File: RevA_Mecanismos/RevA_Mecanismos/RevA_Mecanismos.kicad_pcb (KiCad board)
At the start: 4 copper layers, 80 x 80 mm, 84 parts, among them IC1 MAX33040EAKA+T, J1 PROG, J10 Conn_01x02_Pin, J2 Conn_01x03_Pin, J3 430450224, J4 430450224, J5 DEBUG_CONN, J6 430450224, J7 430450224, J8 Conn_01x08_Pin, J9 Conn_01x02_Pin, Q1 NDS352AP, SW1 SW_Push, U1 STM32L431RCTx, U2 R-78E3.3-1.0, U3 R-78E5.0-1.0, Y1 16MHz

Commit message: Adiciones a secciones de motores y power supply para placa de mecanismos
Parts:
- moved G*** 7.66 mm to (203.2, 129.5)
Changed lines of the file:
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@@
   )
   (footprint "footprints:sticker" (layer "B.Cu")
-    (at 203.7 121.9 180)
+    (at 203.2 129.54 180)
     (attr board_only exclude_from_pos_files exclude_from_bom)
     (fp_text reference "G***" (at 0 0) (layer "B.SilkS") hide

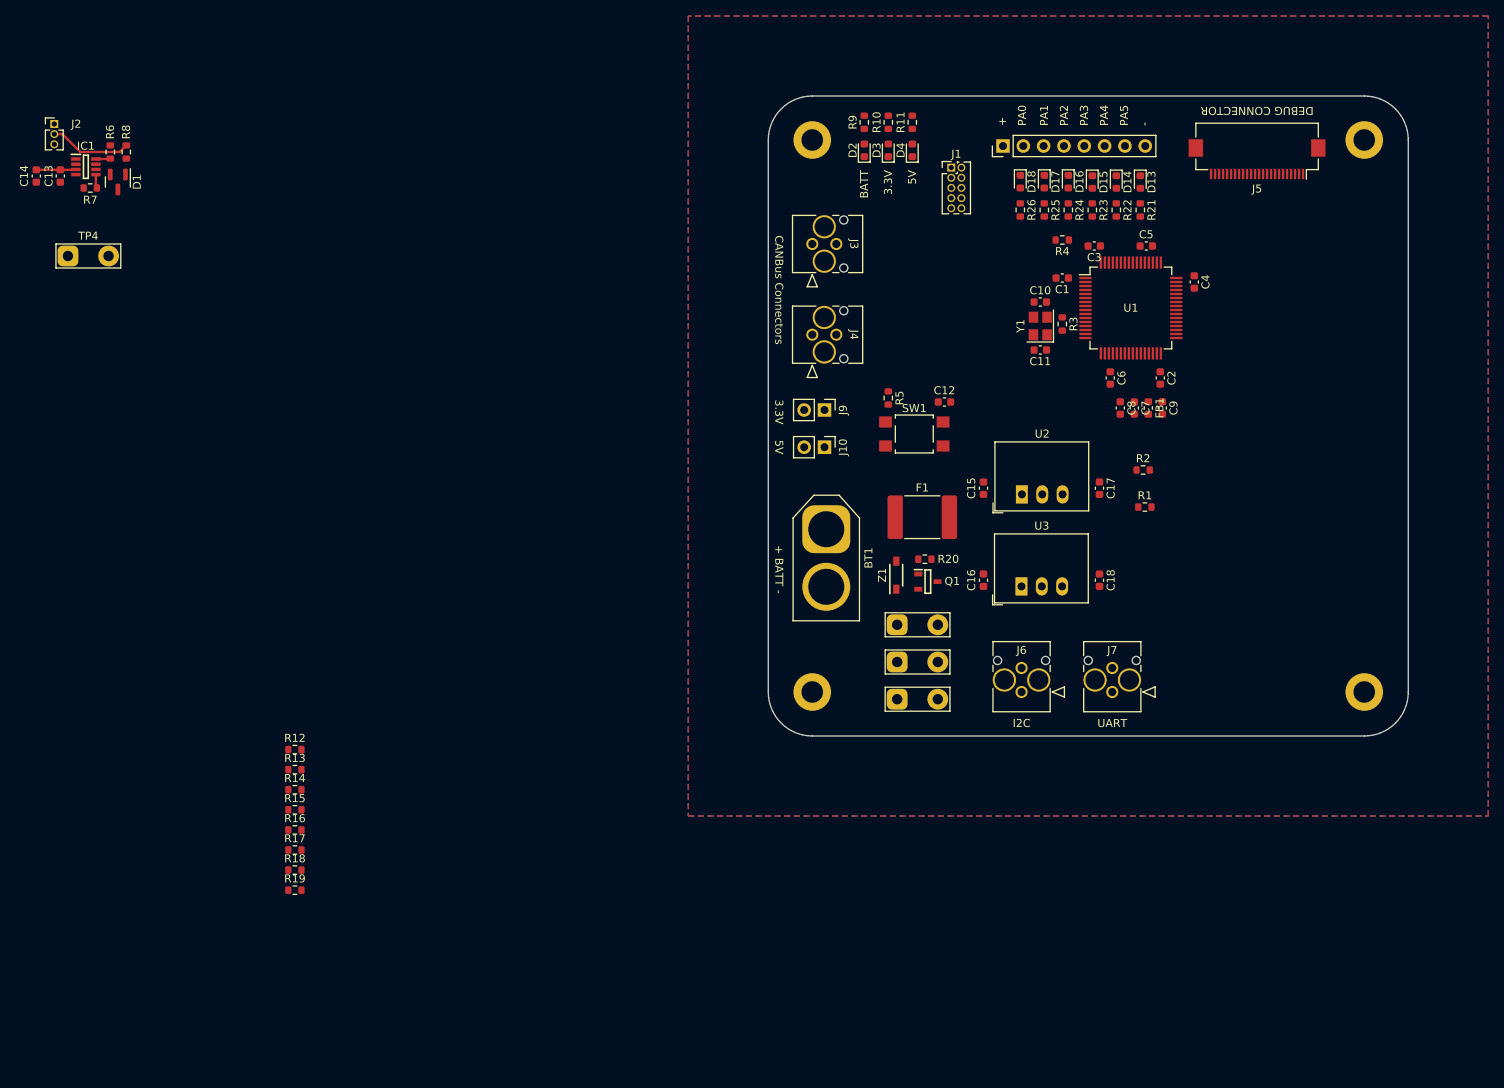
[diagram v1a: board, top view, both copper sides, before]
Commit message: Updated STM32 USV Mechanism PCB
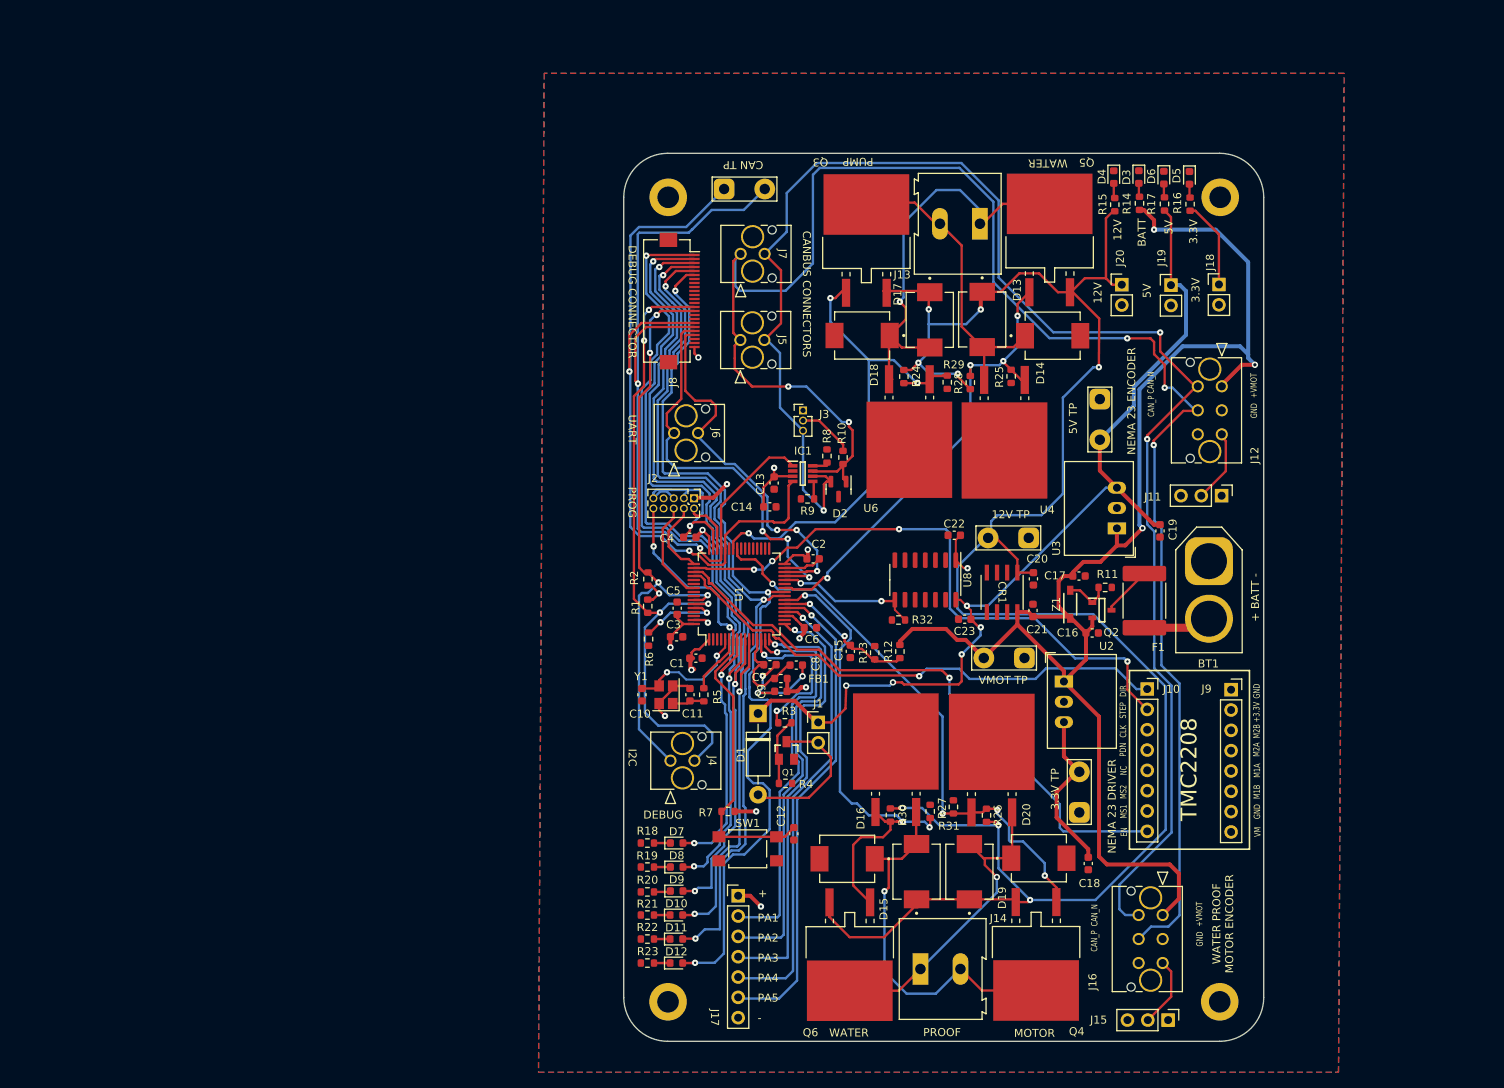
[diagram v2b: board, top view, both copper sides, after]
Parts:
- removed the J8 at (154.3, 31.2)
- removed the R14 at (65.8, 111.7)
- removed the R16 at (65.8, 116.7)
- removed the R17 at (65.8, 119.2)
- removed the R18 at (65.8, 121.8)
- removed the R19 at (65.8, 124.3)
- added C15: 3.3u, Capacitor_SMD:C_0603_1608Metric, F.Cu at (135.3, 94.4)
- added C20: 0.1u, Capacitor_SMD:C_0603_1608Metric, F.Cu at (158.1, 85.4)
- added C21: 0.33u, Capacitor_SMD:C_0603_1608Metric, F.Cu at (158.1, 89.3)
- added C22: 0.1u, Capacitor_SMD:C_0603_1608Metric, F.Cu at (148.2, 79.9)
- added C23: 0.1u, Capacitor_SMD:C_0603_1608Metric, F.Cu at (149.6, 90.4)
- added CR1: L78L12ABD-TR, L78L12ABD-TR:SO-8_STM, F.Cu at (154.2, 87.0)
- added D1: 1N4001, Diode_THT:D_DO-41_SOD81_P10.16mm_Horizontal, F.Cu at (123.7, 102.2)
- added D13: SS34, SS34:DIOM7959X265N, F.Cu at (151.7, 52.9)
- added D14: SS34, SS34:DIOM7959X265N, F.Cu at (160.5, 55.0)
- added D15: SS34, SS34:DIOM7959X265N, F.Cu at (143.5, 122.0)
- added D16: SS34, SS34:DIOM7959X265N, F.Cu at (134.9, 120.4)
- added D17: SS34, SS34:DIOM7959X265N, F.Cu at (145.2, 53.0)
- added D18: SS34, SS34:DIOM7959X265N, F.Cu at (136.7, 54.9)
- added D19: SS34, SS34:DIOM7959X265N, F.Cu at (150.1, 122.0)
- added D20: SS34, SS34:DIOM7959X265N, F.Cu at (158.8, 120.3)
- added D4: BAT_OK, LED_SMD:LED_0603_1608Metric, F.Cu at (168.2, 35.1)
- added J10: Conn_01x08_Socket, Connector_PinSocket_2.54mm:PinSocket_1x08_P2.54mm_Vertical, F.Cu at (172.4, 99.1)
- added J11: Conn_01x03_Pin, Connector_PinHeader_2.54mm:PinHeader_1x03_P2.54mm_Vertical, F.Cu at (181.7, 75.0)
- added J12: 430450624, MolexConnectors:CON_430450624_MOL, F.Cu at (181.7, 61.3)
- added J13: Screw_Terminal_01x02, TerminalBlock:TerminalBlock_Altech_AK300-2_P5.00mm, F.Cu at (151.5, 41.0)
- added J14: Screw_Terminal_01x02, TerminalBlock:TerminalBlock_Altech_AK300-2_P5.00mm, F.Cu at (144.0, 134.1)
- added J15: Conn_01x03_Pin, Connector_PinHeader_2.54mm:PinHeader_1x03_P2.54mm_Vertical, F.Cu at (175.0, 140.5)
- added J16: 430450624, MolexConnectors:CON_430450624_MOL, F.Cu at (174.3, 127.4)
- added J17: Conn_01x07_Pin, Connector_PinHeader_2.54mm:PinHeader_1x07_P2.54mm_Vertical, F.Cu at (121.2, 125.0)
- added J2: PROG, Connector_PinHeader_1.27mm:PinHeader_2x05_P1.27mm_Vertical, F.Cu at (115.7, 75.3)
- added J20: Conn_01x02_Pin, Connector_PinHeader_2.54mm:PinHeader_1x02_P2.54mm_Vertical, F.Cu at (169.2, 48.6)
- added J9: Conn_01x08_Socket, Connector_PinSocket_2.54mm:PinSocket_1x08_P2.54mm_Vertical, F.Cu at (182.9, 99.2)
- added Q1: FDN335N, FDN335N:SSOT-3, F.Cu at (127.3, 106.8)
- added Q3: IRF9540NSPBF, IRF9540NSPBF:PMOSGDS_D2PAK_INF, F.Cu at (137.3, 41.6)
- added Q4: IRF9540NSPBF, IRF9540NSPBF:PMOSGDS_D2PAK_INF, F.Cu at (158.5, 133.8)
- added Q5: IRF9540NSPBF, IRF9540NSPBF:PMOSGDS_D2PAK_INF, F.Cu at (160.2, 41.5)
- added Q6: IRF9540NSPBF, IRF9540NSPBF:PMOSGDS_D2PAK_INF, F.Cu at (135.2, 133.8)
- added R24: 750, Resistor_SMD:R_0603_1608Metric, F.Cu at (141.9, 60.1)
- added R25: 750, Resistor_SMD:R_0603_1608Metric, F.Cu at (155.4, 60.0)
- added R26: 750, Resistor_SMD:R_0603_1608Metric, F.Cu at (152.3, 114.9)
- added R27: 750, Resistor_SMD:R_0603_1608Metric, F.Cu at (145.2, 114.4)
- added R28: 750, Resistor_SMD:R_0603_1608Metric, F.Cu at (150.3, 60.8)
- added R29: 750, Resistor_SMD:R_0603_1608Metric, F.Cu at (147.4, 60.8)
- added R3: 220, Resistor_SMD:R_0603_1608Metric, F.Cu at (127.1, 103.4)
- added R30: 750, Resistor_SMD:R_0603_1608Metric, F.Cu at (140.3, 114.9)
- added R31: 750, Resistor_SMD:R_0603_1608Metric, F.Cu at (148.1, 113.9)
- added R32: R, Resistor_SMD:R_0603_1608Metric, F.Cu at (141.3, 90.5)
- added R4: 47k, Resistor_SMD:R_0603_1608Metric, F.Cu at (127.2, 110.9)
- added TP1: TestPoint_2Pole, TestPoint:TestPoint_2Pads_Pitch5.08mm_Drill1.3mm, F.Cu at (157.6, 80.2)
- added U4: IRF540SPBF, IRF540SPBF:D2PAK_VIS, F.Cu at (154.5, 69.3)
- added U5: IRF540SPBF, IRF540SPBF:D2PAK_VIS, F.Cu at (140.9, 105.7)
- added U6: IRF540SPBF, IRF540SPBF:D2PAK_VIS, F.Cu at (142.6, 69.2)
- added U7: IRF540SPBF, IRF540SPBF:D2PAK_VIS, F.Cu at (152.9, 105.7)
- added U8: TXB0104D, Package_SO:SOIC-14_3.9x8.7mm_P1.27mm, F.Cu at (144.6, 85.5)
- J1: value PROG -> Conn_01x02_Socket; footprint Connector_PinHeader_1.27mm:PinHeader_2x05_P1.27mm_Vertical -> Connector_PinHeader_2.54mm:PinHeader_1x02_P2.54mm_Vertical
- R12: value 750 -> 34.8k
- R13: value 750 -> 10k
- moved G*** 159.2 mm to (60.8, 58.4)
- moved R15 127.4 mm to (168.3, 38.6), turned to -90 degrees
- moved D12 106.7 mm to (113.5, 133.4), turned to 0 degrees
- moved D11 105.2 mm to (113.5, 130.4), turned to 0 degrees
- moved R23 105.0 mm to (109.9, 133.4), turned to 180 degrees
- moved D10 103.9 mm to (113.5, 127.4), turned to 0 degrees
- moved R22 103.8 mm to (109.9, 130.4), turned to 180 degrees
- moved D9 102.7 mm to (113.6, 124.4), turned to 0 degrees
- moved R21 102.6 mm to (109.9, 127.4), turned to 180 degrees
- moved R20 101.8 mm to (109.9, 124.5), turned to 180 degrees
- moved D8 101.7 mm to (113.6, 121.4), turned to 0 degrees
- moved D7 100.9 mm to (113.6, 118.4), turned to 0 degrees
- moved R19 100.9 mm to (109.9, 121.4), turned to 180 degrees
- moved C14 100.6 mm to (125.2, 76.4), turned to 0 degrees
- moved R18 100.3 mm to (109.9, 118.4), turned to 180 degrees
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- renumbered C15 to C16, C16 to C17, C17 to C18, C18 to C19, D16 to D10, D17 to D11, D18 to D12, D1 to D2, D2 to D3, D3 to D5, D4 to D6, D13 to D7, D14 to D8, D15 to D9, J9 to J18, J10 to J19, J2 to J3, J6 to J4, J3 to J5, J7 to J6, J4 to J7, J5 to J8, Q1 to Q2, R8 to R10, R20 to R11, R9 to R14, R10 to R16, R11 to R17, R21 to R18, R22 to R19, R23 to R20, R24 to R21, R25 to R22, R26 to R23, R3 to R5, R4 to R6, R5 to R7, R6 to R8, R7 to R9, TP3 to TP2, TP1 to TP3, TP2 to TP4, TP4 to TP5
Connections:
- J1 pad 1: +3.3V -> +5V
- J1 pad 2: SWDIO -> Net-(D1-A)
- R12 pad 1: GND -> +VMOT
- R12 pad 2: TIM1_CH1N -> VREAD
- R13 pad 1: TIM1_CH1 -> VREAD
- R13 pad 2: unconnected-(R13-Pad2) -> GND
- R15 pad 1: GND -> Net-(D4-A)
- R15 pad 2: TIM1_CH1 -> +12V
- U1 pad 10: unconnected-(U1-PC2-Pad10) -> DEBUG_3
- U1 pad 11: unconnected-(U1-PC3-Pad11) -> DEBUG_4
- U1 pad 22: unconnected-(U1-PA6-Pad22) -> VREAD
- U1 pad 23: TIM1_CH1N -> WPM_TIM1_CH1N
- U1 pad 24: unconnected-(U1-PC4-Pad24) -> DEBUG_5
- U1 pad 25: unconnected-(U1-PC5-Pad25) -> DEBUG_6
- U1 pad 26: unconnected-(U1-PB0-Pad26) -> WP_TIM1_CH2N
- U1 pad 28: unconnected-(U1-PB2-Pad28) -> LEVEL_SHIFTER
- U1 pad 41: TIM1_CH1 -> WPM_TIM1_CH1
- U1 pad 42: unconnected-(U1-PA9-Pad42) -> WP_TIM1_CH2
- U1 pad 50: unconnected-(U1-PA15-Pad50) -> STPR_STEP
- U1 pad 51: unconnected-(U1-PC10-Pad51) -> STPR_EN
- U1 pad 52: unconnected-(U1-PC11-Pad52) -> STPR_DIR
- U1 pad 8: unconnected-(U1-PC0-Pad8) -> DEBUG_1
- U1 pad 9: unconnected-(U1-PC1-Pad9) -> DEBUG_2
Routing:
- net +12V: track 0.00 -> 251.8 mm, vias 0 -> 8
- net CAN_P: track 0.00 -> 214.8 mm, vias 0 -> 5
- net CAN_N: track 0.00 -> 198.4 mm, vias 0 -> 3
- net +VMOT: track 0.00 -> 180.2 mm, vias 0 -> 3
- net +5V: track 0.00 -> 118.2 mm, vias 0 -> 5
- net DEBUG_6: track 0.00 -> 117.2 mm, vias 0 -> 3
- net DEBUG_4: track 0.00 -> 110.1 mm, vias 0 -> 3
- net DEBUG_5: track 0.00 -> 109.1 mm, vias 0 -> 3
- net DEBUG_3: track 0.00 -> 105.8 mm, vias 0 -> 3
- net DEBUG_2: track 0.00 -> 102.0 mm, vias 0 -> 3
- net DEBUG_1: track 0.00 -> 101.4 mm, vias 0 -> 3
- net CAN_TX: track 0.00 -> 99.8 mm, vias 0 -> 2
- net CAN_RX: track 0.00 -> 95.2 mm, vias 0 -> 2
- net +3.3V: track 4.97 -> 90.6 mm, vias 0 -> 13
- net SDA: track 0.00 -> 82.2 mm, vias 0 -> 4
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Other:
- board size 80 x 80 mm -> 80 x 111 mm
- board text added: "+3.3V"
- board text added: "+VMOT"
- board text added: "12V"
- board text added: "12V TP"
- board text added: "3.3V TP"
- board text added: "5V TP"
- board text added: "CAN TP"
- board text added: "CANBUS CONNECTORS"
- board text added: "CAN_N"
- board text added: "CAN_P"
- board text added: "CLK"
- board text added: "DEBUG"
- board text added: "DEBUG CONNECTORS"
- board text added: "DIR"
- board text added: "EN"
- board text added: "GND"
- board text added: "M1A"
- board text added: "M1B"
- board text added: "M2A"
- board text added: "M2B"
- board text added: "MOTOR"
- board text added: "MS1"
- board text added: "MS2"
- board text added: "NC"
- board text added: "NEMA 23 DRIVER"
- board text added: "NEMA 23 ENCODER"
- board text added: "PDN"
- board text added: "PROG"
- board text added: "PROOF"
- board text added: "PUMP"
- board text added: "R30"
- board text added: "STEP"
- board text added: "TMC2208"
- board text added: "VM"
- board text added: "VMOT TP"
- board text added: "WATER"
- board text added: "WATER PROOF MOTOR ENCODER"
- board text removed: "CAN TRANSCIEVER"
- board text removed: "CANBus Connectors"
- board text removed: "HBRIDGE"
- board text removed: "PA0"
- board text removed: "STEPPER DRIVERS"
- board text removed: "STEPPER OUTPUTS"

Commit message: Complete schematic and pcb designs, routes missing and not yet complete
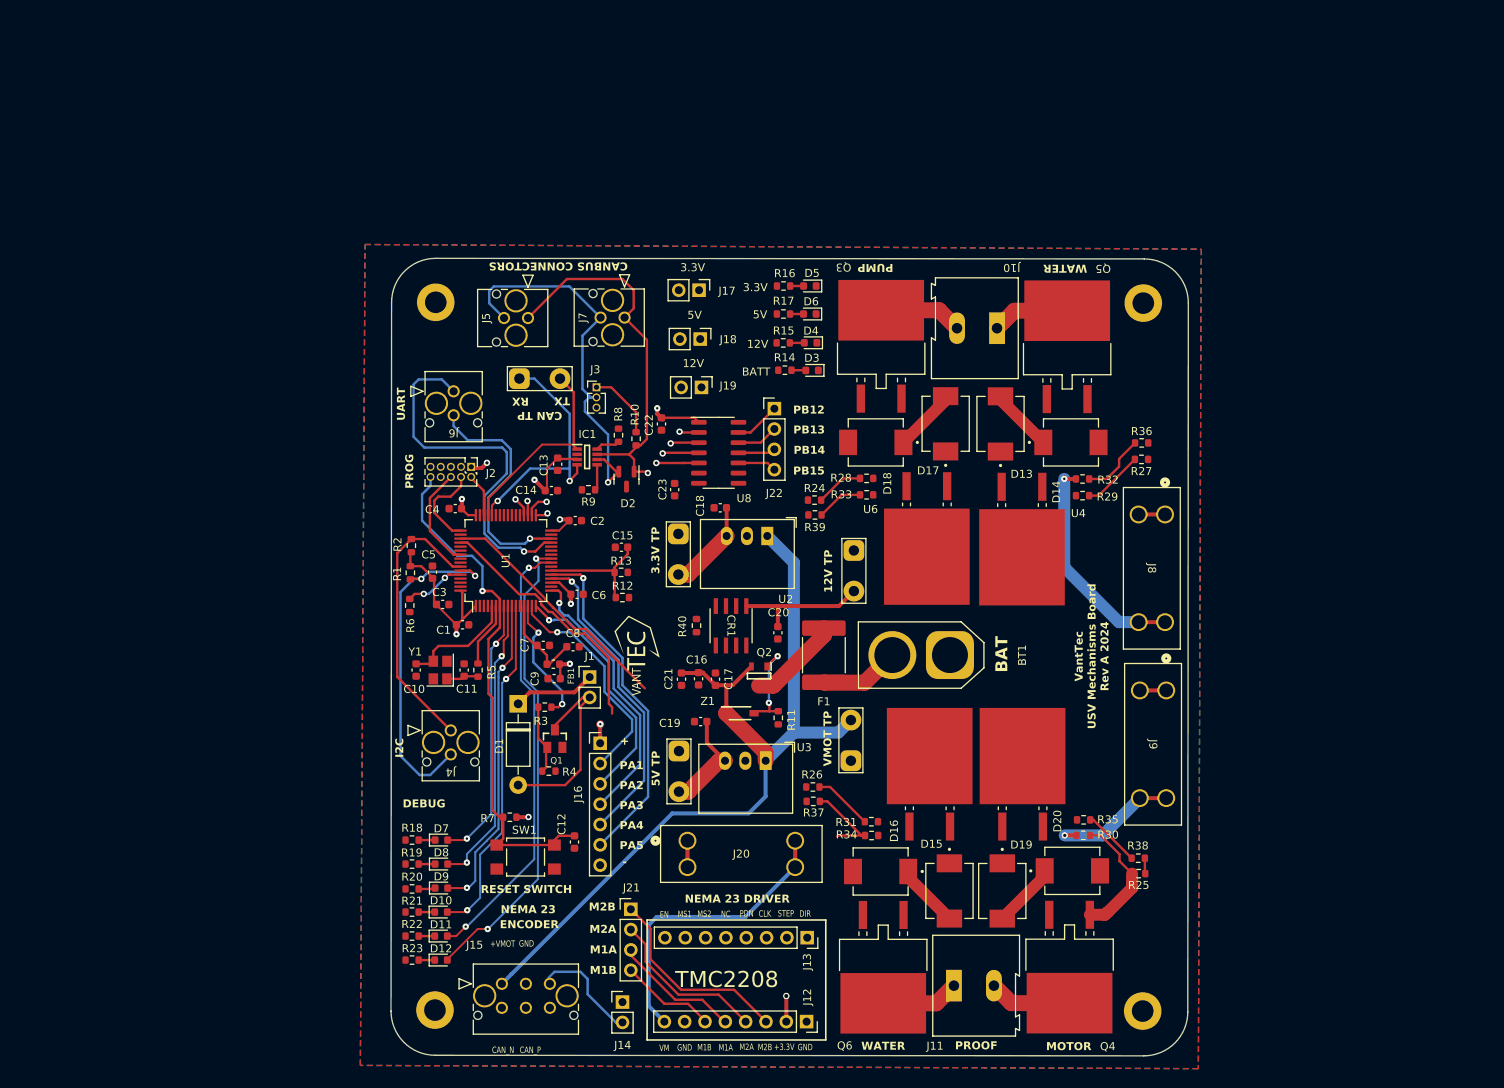
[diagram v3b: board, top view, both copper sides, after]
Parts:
- removed the G*** at (60.8, 58.4)
- removed the J11 at (181.7, 75.0)
- removed the J15 at (175.0, 140.5)
- removed the J16 at (174.3, 127.4)
- added G***: LOGO, VANTTEC:vanttec_logo_10mm_5.7mm, F.Cu at (108.6, 95.0)
- added J14: Conn_01x02_Pin, Connector_PinHeader_2.54mm:PinHeader_1x02_P2.54mm_Vertical, F.Cu at (106.8, 138.3)
- added J20: 3557-2, 36-3557-2-ND:CONN_3557-2_KEY, F.Cu at (114.9, 118.1)
- added J21: Conn_01x04_Pin, Connector_PinHeader_2.54mm:PinHeader_1x04_P2.54mm_Vertical, F.Cu at (107.8, 126.7)
- added J22: Conn_01x04_Pin, Connector_PinHeader_2.54mm:PinHeader_1x04_P2.54mm_Vertical, F.Cu at (125.8, 64.1)
- added J9: 3557-2, 36-3557-2-ND:CONN_3557-2_KEY, F.Cu at (174.7, 99.3)
- added R24: 100, Resistor_SMD:R_0603_1608Metric, F.Cu at (130.8, 75.5)
- added R25: 100, Resistor_SMD:R_0603_1608Metric, F.Cu at (171.3, 122.2)
- added R26: 100, Resistor_SMD:R_0603_1608Metric, F.Cu at (130.6, 111.4)
- added R27: 100, Resistor_SMD:R_0603_1608Metric, F.Cu at (171.7, 70.4)
- added R36: 100, Resistor_SMD:R_0603_1608Metric, F.Cu at (171.7, 68.4)
- added R37: 100, Resistor_SMD:R_0603_1608Metric, F.Cu at (130.6, 113.2)
- added R38: 100, Resistor_SMD:R_0603_1608Metric, F.Cu at (171.2, 120.3)
- added R39: 100, Resistor_SMD:R_0603_1608Metric, F.Cu at (130.8, 77.4)
- J3: value Conn_01x03_Pin -> Conn_01x02_Pin
- J8: value DEBUG_CONN -> 3557-2; footprint Connector_FFC-FPC:Hirose_FH12-24S-0.5SH_1x24-1MP_P0.50mm_Horizontal -> 36-3557-2-ND:CONN_3557-2_KEY
- R28: renamed from R24; value 750 -> 10k
- R29: renamed from R25; value 750 -> 10k
- R30: renamed from R26; value 750 -> 10k
- R31: renamed from R27; value 750 -> 10k
- R32: renamed from R28; value 750 -> 10k
- R33: renamed from R29; value 750 -> 10k
- R34: renamed from R30; value 750 -> 10k
- R35: renamed from R31; value 750 -> 10k
- moved J15 116.9 mm to (91.7, 136.0), turned to 180 degrees
- moved H3 105.7 mm to (83.4, 139.3)
- moved H1 98.9 mm to (83.4, 50.8)
- moved H2 87.9 mm to (171.9, 50.9)
- moved TP2 68.6 mm to (113.8, 106.9)
- moved J12 67.4 mm to (129.8, 140.7), turned to -90 degrees
- moved J8 66.3 mm to (174.6, 77.3)
- moved J17 65.0 mm to (116.3, 49.3), turned to -90 degrees
- moved C18 64.0 mm to (119.0, 76.5), turned to 0 degrees
- moved C19 62.2 mm to (116.5, 103.2), turned to 0 degrees
- moved TP3 61.0 mm to (113.8, 79.7), turned to -90 degrees
- moved H4 59.3 mm to (171.8, 139.4)
- moved J18 59.2 mm to (116.5, 55.4), turned to -90 degrees
- moved J19 54.1 mm to (116.7, 61.4), turned to -90 degrees
- moved J13 52.6 mm to (129.9, 130.2), turned to -90 degrees
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- renumbered H2 to H1, H3 to H2, H1 to H3, J13 to J10, J14 to J11, J9 to J12, J10 to J13, J12 to J15, J17 to J16, J18 to J17, J19 to J18, J20 to J19, R32 to R40, U7 to U5, U5 to U7
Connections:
- D13 pad C: +12V -> Net-(Q3-S)
- D15 pad C: +12V -> Net-(Q4-S)
- D17 pad C: +12V -> Net-(Q3-S)
- D19 pad C: +12V -> Net-(Q4-S)
- J12 pad 8: VM -> Net-(J12-Pin_8)
- J13 pad 3: CLK -> unconnected-(J13-Pin_3-Pad3)
- J13 pad 4: PDN -> unconnected-(J13-Pin_4-Pad4)
- J13 pad 5: NC -> unconnected-(J13-Pin_5-Pad5)
- J13 pad 6: MS2 -> unconnected-(J13-Pin_6-Pad6)
- J13 pad 7: MS1 -> unconnected-(J13-Pin_7-Pad7)
- J3 pad 1: unconnected-(J3-Pin_1-Pad1) -> Net-(J3-Pin_1)
- J3 pad 2: Net-(J3-Pin_2) -> CAN_N
- J3 pad 3: CAN_N -> (no net)
- J8 pad 1: DEBUG_1 -> +12V
- J8 pad 2: DEBUG_2 -> +12V
- J8 pad 3: DEBUG_3 -> Net-(Q3-S)
- J8 pad 4: DEBUG_4 -> Net-(Q3-S)
- Q3 pad 1: WP_TIM1_CH2 -> Net-(Q3-G)
- Q3 pad 3: +12V -> Net-(Q3-S)
- Q4 pad 1: WPM_TIM1_CH1 -> Net-(Q4-G)
- Q4 pad 3: +12V -> Net-(Q4-S)
- Q5 pad 1: WP_TIM1_CH2N -> Net-(Q5-G)
- Q5 pad 3: +12V -> Net-(Q3-S)
- Q6 pad 1: WPM_TIM1_CH1N -> Net-(Q6-G)
- Q6 pad 3: +12V -> Net-(Q4-S)
- R10 pad 2: Net-(J3-Pin_2) -> Net-(J3-Pin_1)
- R28 pad 1: WP_TIM1_CH2 -> Net-(Q3-G)
- R28 pad 2: +12V -> Net-(Q3-S)
- R29 pad 2: WP_TIM1_CH2N -> Net-(U4-G)
- R30 pad 1: WPM_TIM1_CH1 -> Net-(Q4-G)
- R30 pad 2: +12V -> Net-(Q4-S)
- R31 pad 2: WPM_TIM1_CH1N -> Net-(U5-G)
- R32 pad 1: WP_TIM1_CH2N -> Net-(Q5-G)
- R32 pad 2: +12V -> Net-(Q3-S)
- R33 pad 2: WP_TIM1_CH2 -> Net-(U6-G)
- R34 pad 1: WPM_TIM1_CH1N -> Net-(Q6-G)
- R34 pad 2: +12V -> Net-(Q4-S)
- R35 pad 2: WPM_TIM1_CH1 -> Net-(U7-G)
- U1 pad 33: unconnected-(U1-PB12-Pad33) -> IO_7
- U1 pad 34: unconnected-(U1-PB13-Pad34) -> IO_8
- U1 pad 35: unconnected-(U1-PB14-Pad35) -> IO_9
- U1 pad 36: unconnected-(U1-PB15-Pad36) -> IO_10
- U4 pad 1: WP_TIM1_CH2N -> Net-(U4-G)
- U5 pad 1: WPM_TIM1_CH1 -> Net-(U5-G)
- U5 pad 3: WPM_- -> WPM_+
- U6 pad 1: WP_TIM1_CH2 -> Net-(U6-G)
- U7 pad 1: WPM_TIM1_CH1N -> Net-(U7-G)
- U7 pad 3: WPM_+ -> WPM_-
- U8 pad 2: CA1 -> IO_7
- U8 pad 3: CA2 -> IO_8
- U8 pad 4: CA3 -> IO_9
- U8 pad 5: CA4 -> IO_10
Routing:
- net +12V: track 251.8 -> 26.7 mm, vias 8 -> 0
- net +5V: track 118.2 -> 23.5 mm, vias 5 -> 0
- net STPR_STEP: track 75.9 -> 0.00 mm, vias 4 -> 0
- net CAN_TX: track 99.8 -> 26.0 mm, vias 2 -> 0
- net +VMOT: track 180.2 -> 107.8 mm, vias 3 -> 0
- net WPM_TIM1_CH1: track 70.7 -> 1.95 mm, vias 4 -> 0
- net DEBUG_1: track 101.4 -> 33.6 mm, vias 3 -> 2
- net DEBUG_4: track 110.1 -> 43.2 mm, vias 3 -> 2
- net CAN_P: track 214.8 -> 149.1 mm, vias 5 -> 1
- net DEBUG_3: track 105.8 -> 40.1 mm, vias 3 -> 2
- net DEBUG_2: track 102.0 -> 36.7 mm, vias 3 -> 2
- net WPM_TIM1_CH1N: track 64.3 -> 0.00 mm, vias 3 -> 0
- net CAN_RX: track 95.2 -> 32.2 mm
- net CAN_N: track 198.4 -> 136.3 mm, vias 3 -> 1
- net WP_TIM1_CH2: track 62.0 -> 0.00 mm, vias 3 -> 0
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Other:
- board size 80 x 111 mm -> 99.7 x 99.7 mm
- board text added: "BAT"
- board text added: "ENCODER"
- board text added: "NEMA 23"
- board text added: "PB12"
- board text added: "PB13"
- board text added: "PB14"
- board text added: "PB15"
- board text added: "RESET SWITCH"
- board text added: "RX"
- board text added: "TX"
- board text added: "VantTec USV Mechanisms Board Rev A 2024"
- board text removed: "+ BATT -"
- board text removed: "DEBUG CONNECTOR"
- board text removed: "NEMA 23 ENCODER"
- board text removed: "R30"
- board text removed: "WATER PROOF MOTOR ENCODER"
